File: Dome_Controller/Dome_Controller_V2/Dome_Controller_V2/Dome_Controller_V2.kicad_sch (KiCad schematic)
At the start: 37 parts, among them J1 USB_B_Micro, J13 DB25_Female_MountingHoles, J14 DC-005-5A-2.0, J2 Servo Header, J5 12IN, J6 RSeries Logics, J7 HP, J8 5V Out 2, J9 5V Out, SW1 SW_Push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

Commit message: Added a lot since last check in
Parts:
- removed J2: Servo Header, Connector_PinHeader_2.54mm:PinHeader_1x06_P2.54mm_Vertical, symbol Connector_Generic:Conn_01x06
- removed J?: FrontHP, Connector_Molex:Molex_KK-254_AE-6410-03A_1x03_P2.54mm_Vertical, symbol Connector_Generic:Conn_01x03
- removed J?: RearHP, Connector_Molex:Molex_KK-254_AE-6410-03A_1x03_P2.54mm_Vertical, symbol Connector_Generic:Conn_01x03
- removed J?: TopHP, Connector_Molex:Molex_KK-254_AE-6410-03A_1x03_P2.54mm_Vertical, symbol Connector_Generic:Conn_01x03
- added U7: PCA9685, Custom:PCA9685, symbol Custom:PCA9685
- J12: renamed from J?; value SERIAL_FU2 -> SERIAL_HP
- gave numbers to parts that had none: 4
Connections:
- net +3.3V: now also U7.11 (VCC), U7.5 (VCC)
- net +5V: now also U7.12 (V+), U7.6 (V+)
- net GND: now also U7.1 (GND), U7.7 (GND)
- net SCL: now also U7.3 (SCL), U7.9 (SCL)
- net SDA: now also U7.10 (SDA), U7.4 (SDA)
- net FRONT_HP: no longer names the net of U1.10 (IO25)
- net REAR_HP: no longer names the net of U1.11 (IO26)
- net RX_FU2 renamed RX_HP
- net RX_PSI: no longer names the net of U1.13 (IO14)
- net TOP_HP: no longer names the net of U1.12 (IO27)
- net TX_FU2 renamed TX_HP
- no-connect marks 33 -> 36
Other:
- moved on the sheet: J16

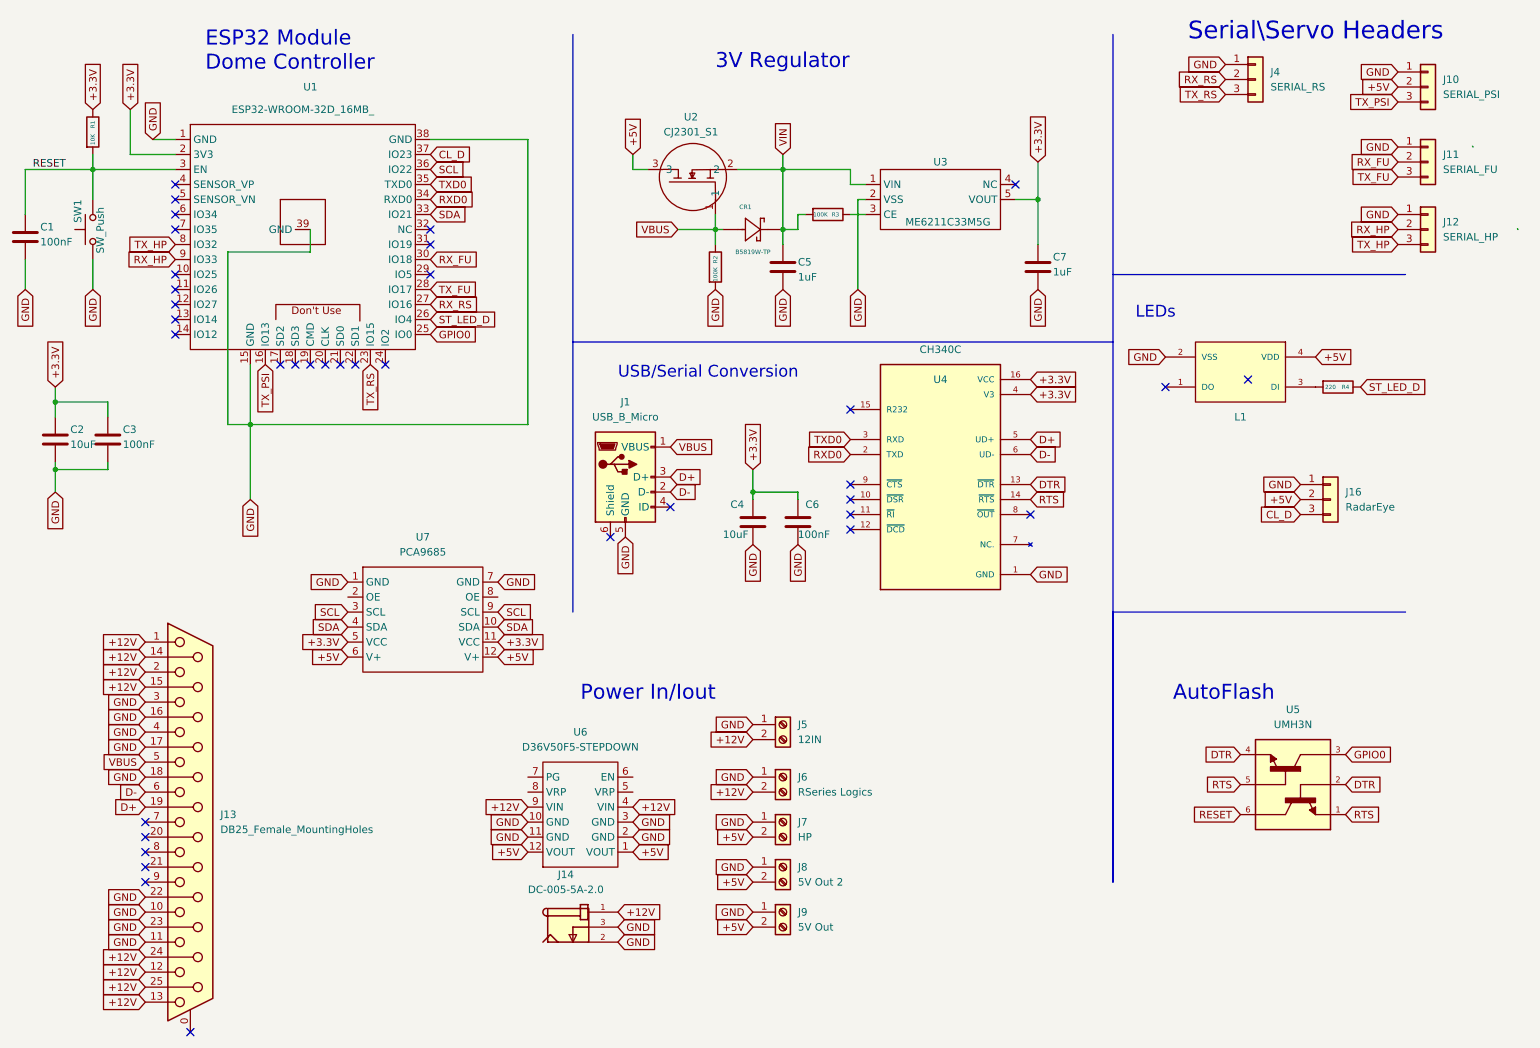
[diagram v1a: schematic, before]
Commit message: added LED PCBs
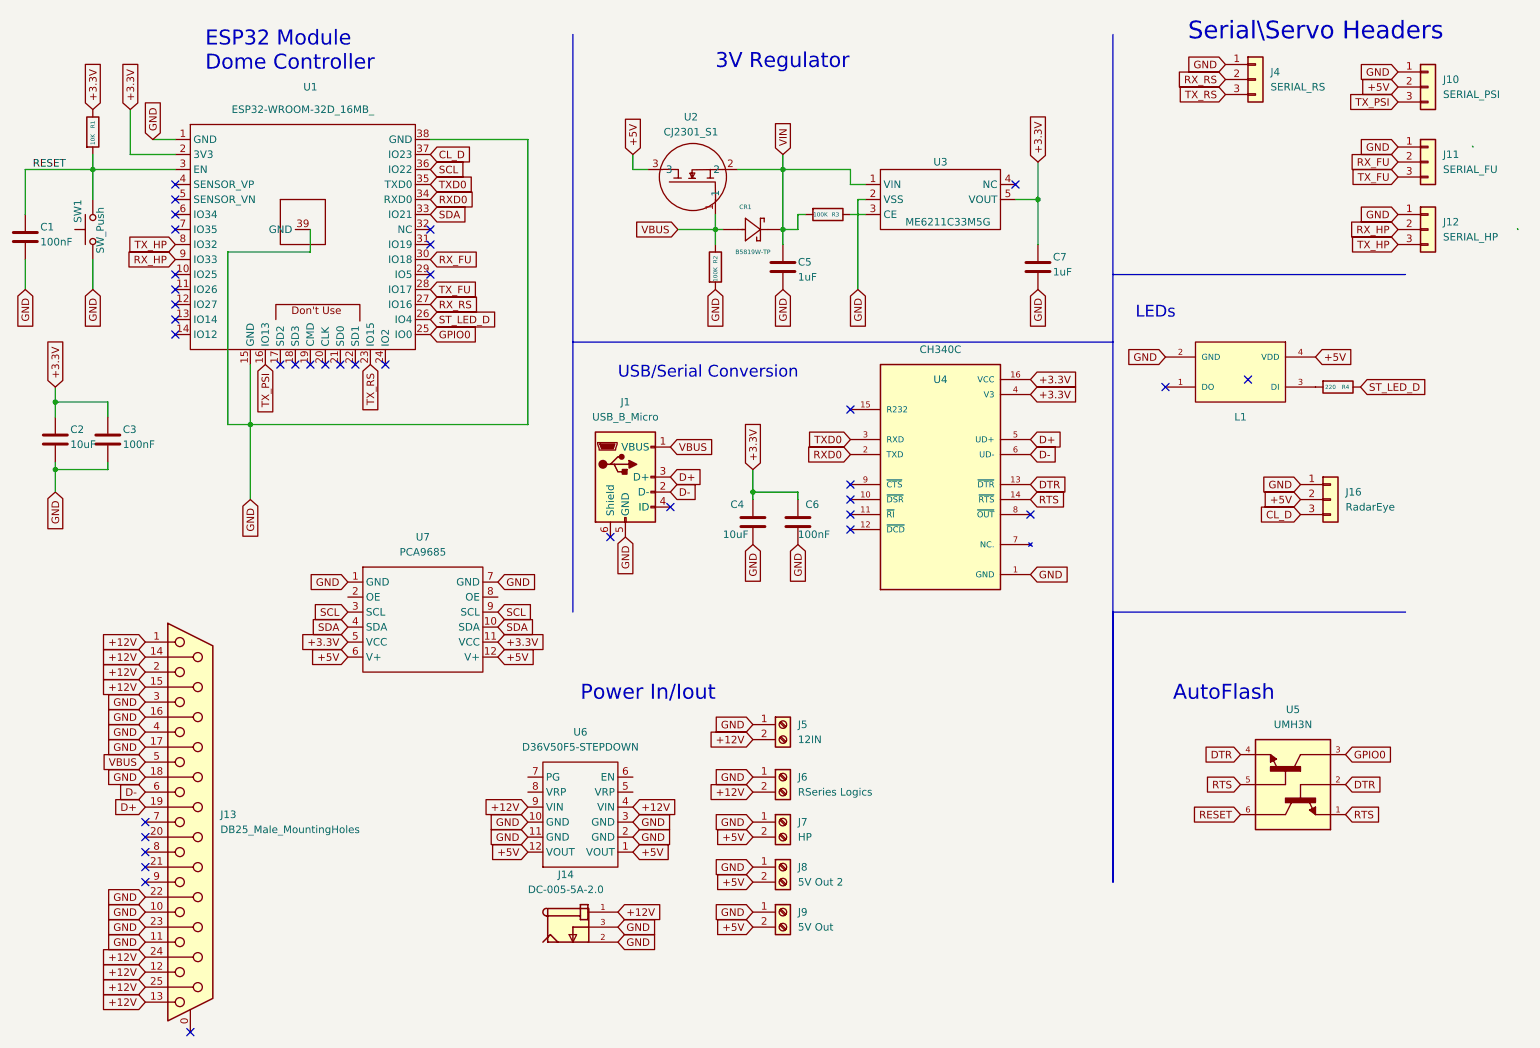
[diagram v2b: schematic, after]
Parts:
- J13: value DB25_Female_MountingHoles -> DB25_Male_MountingHoles; footprint Connector_Dsub:DSUB-25_Female_Vertical_P2.77x2.84mm_MountingHoles -> Connector_Dsub:DSUB-25_Male_Vertical_P2.77x2.84mm_MountingHoles; LCSC C77833 -> C2984302
- J14: LCSC C381116 -> C3010535
- L1: footprint Custom:WS2812B-2020 -> WS2812B-2020
